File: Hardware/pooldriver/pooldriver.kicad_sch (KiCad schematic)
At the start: 44 parts, among them K1 SRD-5VDC-SL-C, K2 SRD-5VDC-SL-C, K3 SRD-5VDC-SL-C, K4 SRD-5VDC-SL-C, K5 SRD-5VDC-SL-C, K6 SRD-5VDC-SL-C, K7 SRD-5VDC-SL-C, M1 DC motoros csap-elzáró, M2 Vízforgató motor, M3 Medence szökőkút motor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

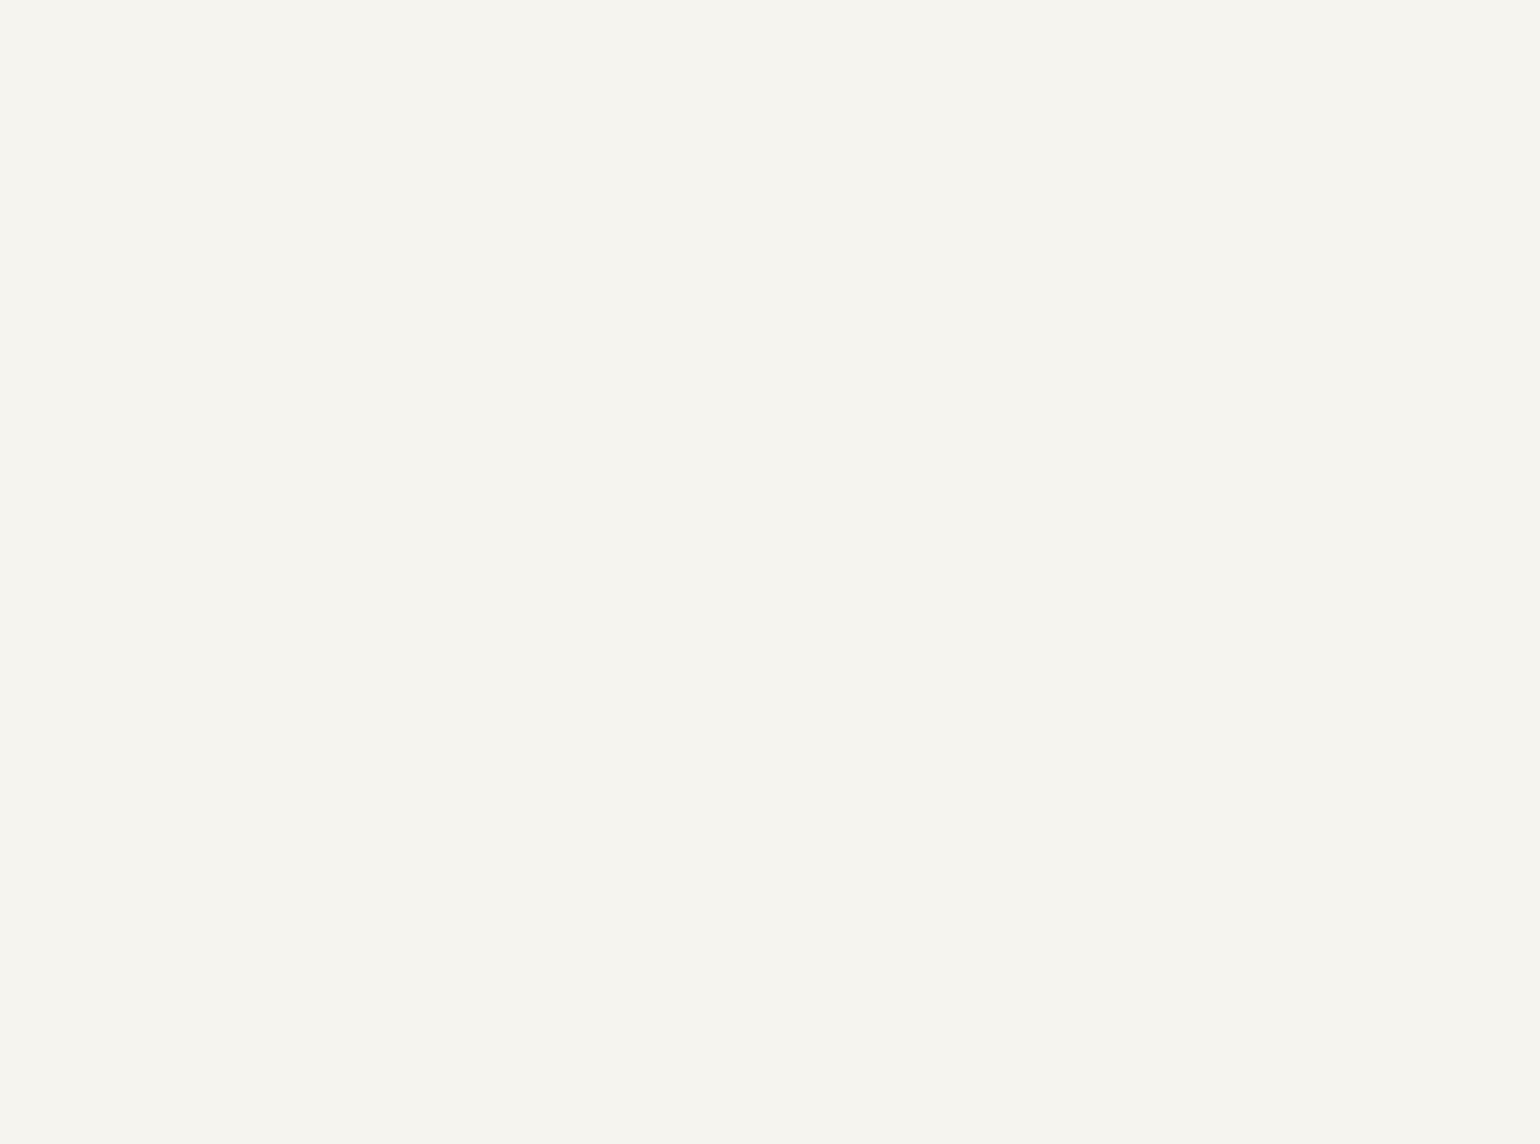
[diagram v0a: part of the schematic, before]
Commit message: mod: relay modules drivers
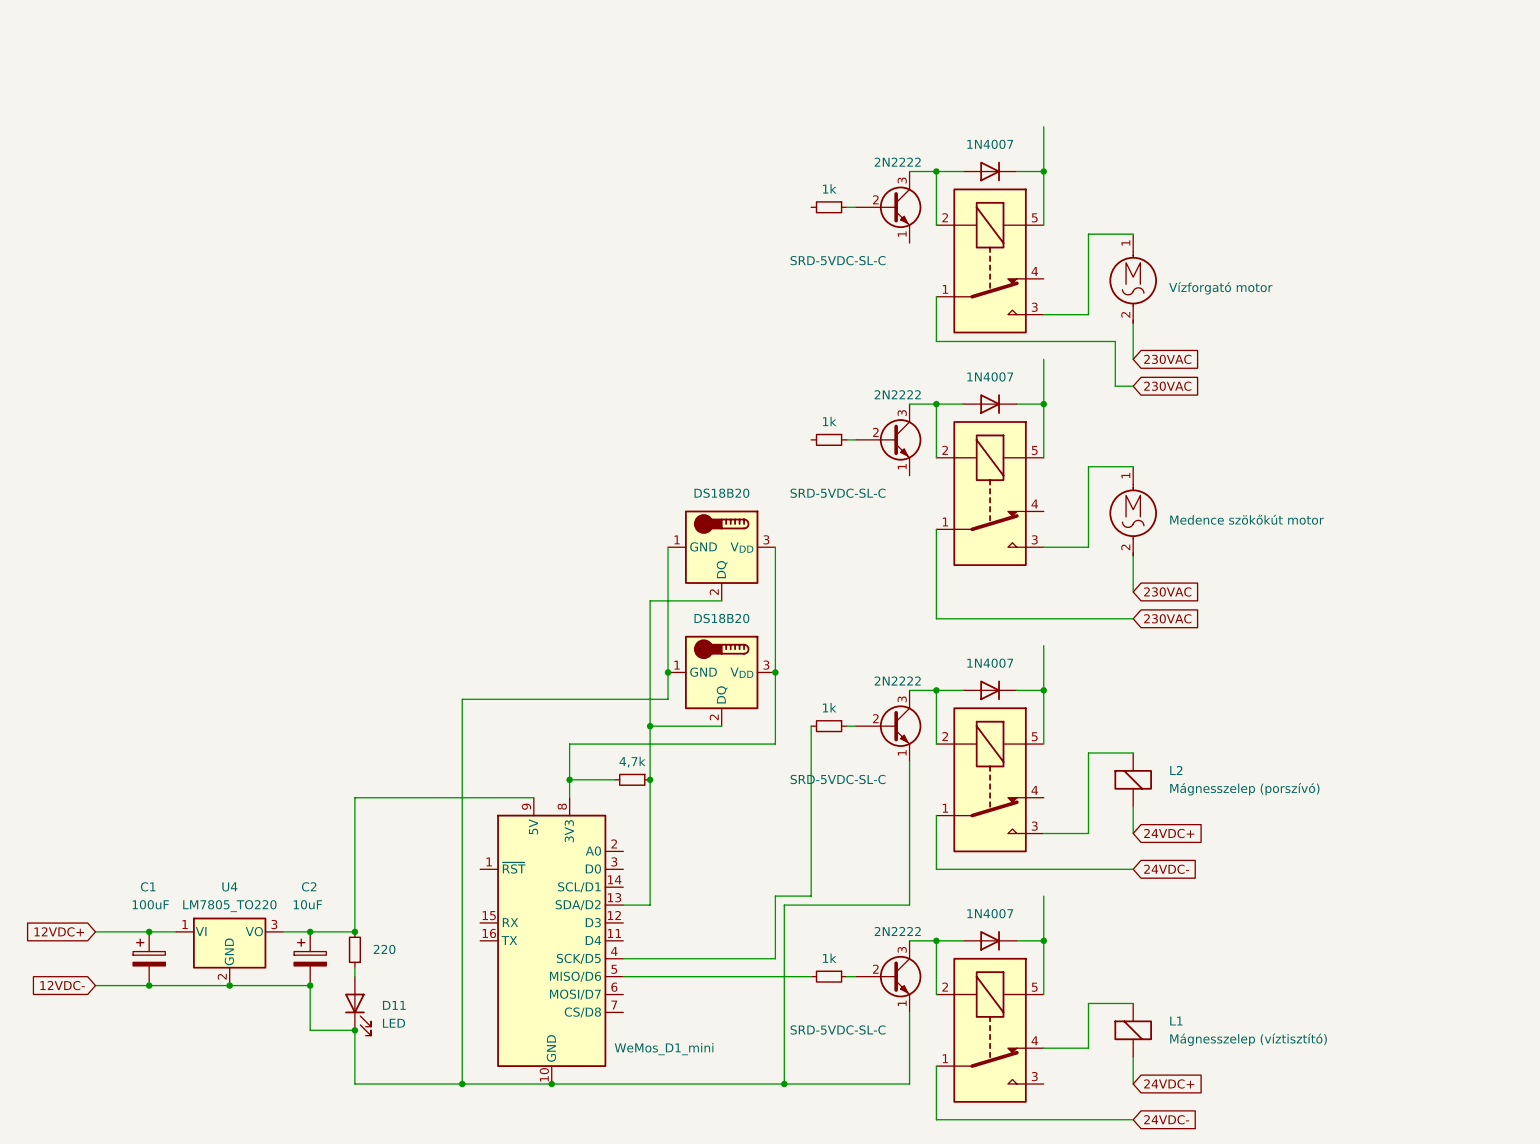
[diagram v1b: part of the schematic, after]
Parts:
- added C1: 100uF, symbol Device:C_Polarized
- added C2: 10uF, symbol Device:C_Polarized
- added D11: LED, symbol Device:LED
- added D12, D13, D14, D15: 1N4007, Diode_THT:D_DO-41_SOD81_P10.16mm_Horizontal, symbol Diode:1N4007
- added K10, K11, K8, K9: SRD-5VDC-SL-C, Relay_THT:Relay_SPDT_SANYOU_SRD_Series_Form_C, symbol Relay:SANYOU_SRD_Form_C
- added L1: Mágnesszelep (víztisztító), symbol Device:ElectromagneticActor
- added L2: Mágnesszelep (porszívó), symbol Device:ElectromagneticActor
- added M4: Vízforgató motor, symbol Motor:Motor_AC
- added M5: Medence szökőkút motor, symbol Motor:Motor_AC
- added Q10, Q11, Q8, Q9: 2N2222, Package_TO_SOT_THT:TO-39-3, symbol Transistor_BJT:2N2219
- added R12: 220, symbol Device:R_Small
- added R13: 4,7k, symbol Device:R_Small
- added R14, R15, R16, R17: 1k, symbol Device:R_Small
- added U4: LM7805_TO220, Package_TO_SOT_THT:TO-220-3_Vertical, symbol Regulator_Linear:LM7805_TO220
- added U6: WeMos_D1_mini, Module:WEMOS_D1_mini_light, symbol MCU_Module:WeMos_D1_mini
- added U7, U8: DS18B20, Package_TO_SOT_THT:TO-92_Inline, symbol Sensor_Temperature:DS18B20
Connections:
- net 12VDC+: now also C1.1, U4.1 (VI)
- net 12VDC-: now also C1.2, C2.2, D11.1 (K), Q8.1 (E), Q9.1 (E), U4.2 (GND), U6.10 (GND), U7.1 (GND), U8.1 (GND)
- net 230VAC: now also K10.1, K11.1, M4.2, M5.2
- new net: Q10.2 (B), R16.1
- new net: D14.2 (A), K10.2, Q10.3 (C)
- new net: D12.1 (K), K8.5
- new net: D12.2 (A), K8.2, Q8.3 (C)
- new net: K10.3, M4.1
- new net: D15.1 (K), K11.5
- new net: D15.2 (A), K11.2, Q11.3 (C)
- new net: K11.3, M5.1
- new net: D14.1 (K), K10.5
- new net: C2.1, R12.2, U4.3 (VO), U6.9 (5V)
- new net: R13.1, U6.13 (SDA/D2), U7.2 (DQ), U8.2 (DQ)
- new net: R13.2, U6.8 (3V3), U7.3 (V_{DD}), U8.3 (V_{DD})
- new net: R15.2, U6.4 (SCK/D5)
- new net: R14.2, U6.5 (MISO/D6)
- new net: Q11.2 (B), R17.1
- new net: K8.4, L1.1 (-)
- new net: Q9.2 (B), R15.1
- new net: D13.2 (A), K9.2, Q9.3 (C)
- new net: D11.2 (A), R12.1
- new net: K9.3, L2.1 (-)
- new net: D13.1 (K), K9.5
- new net: Q8.2 (B), R14.1
- new net 24VDC+: L1.2 (+), L2.2 (+)
- new net 24VDC-: K8.1, K9.1
